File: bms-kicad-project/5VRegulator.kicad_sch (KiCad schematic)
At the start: 39 parts

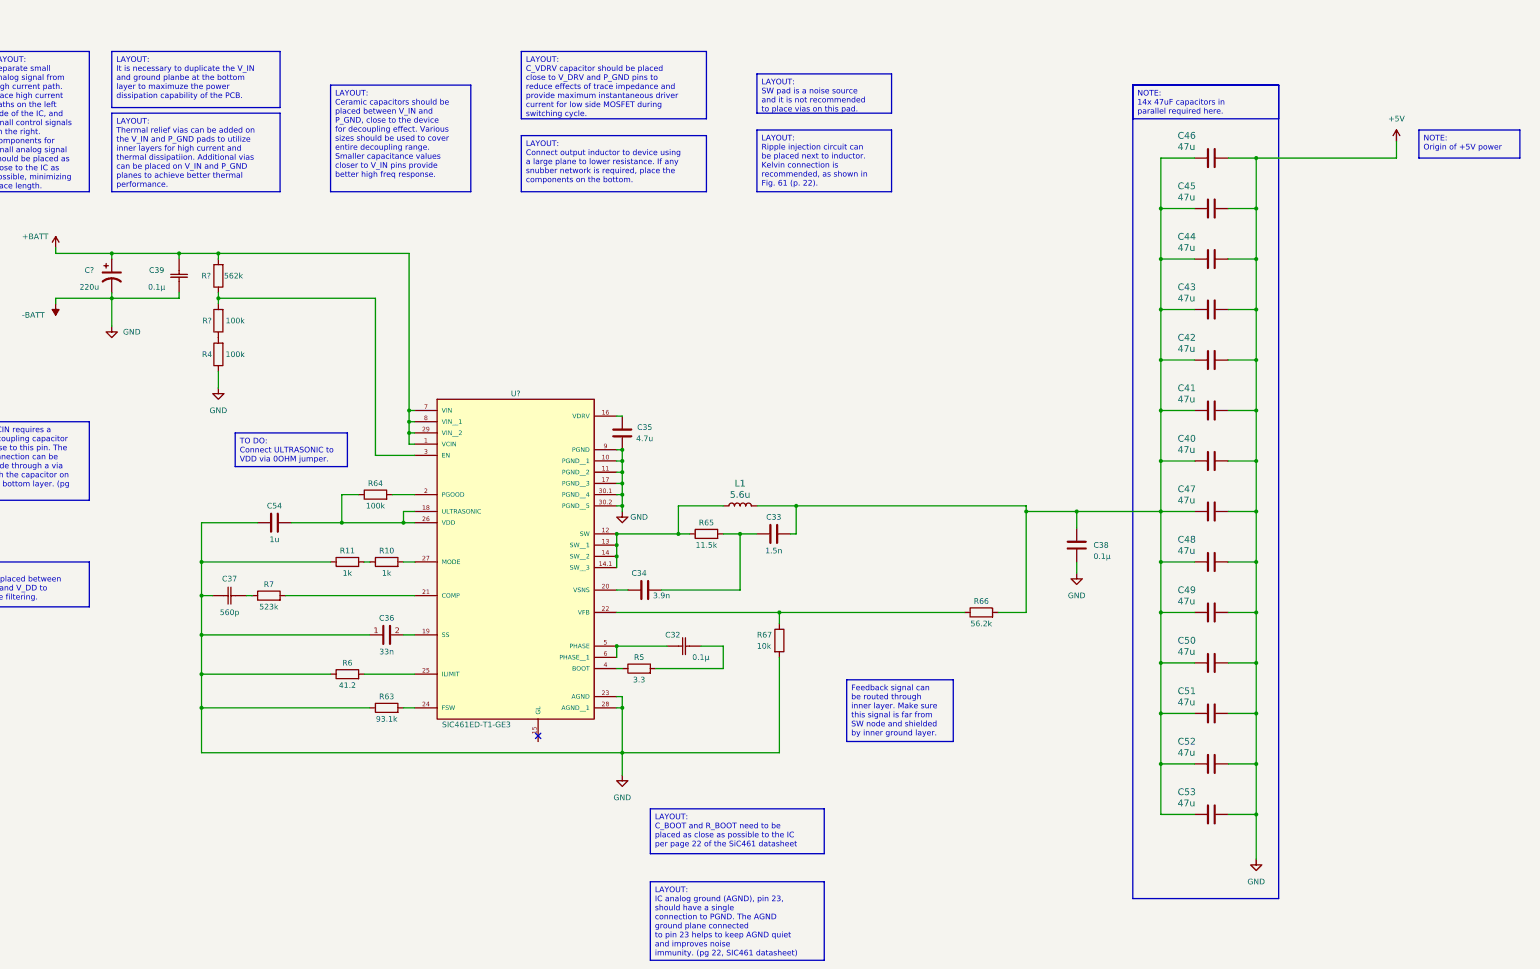
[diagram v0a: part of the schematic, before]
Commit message: feat: Added snubber circuit to 5V Regulator schematic
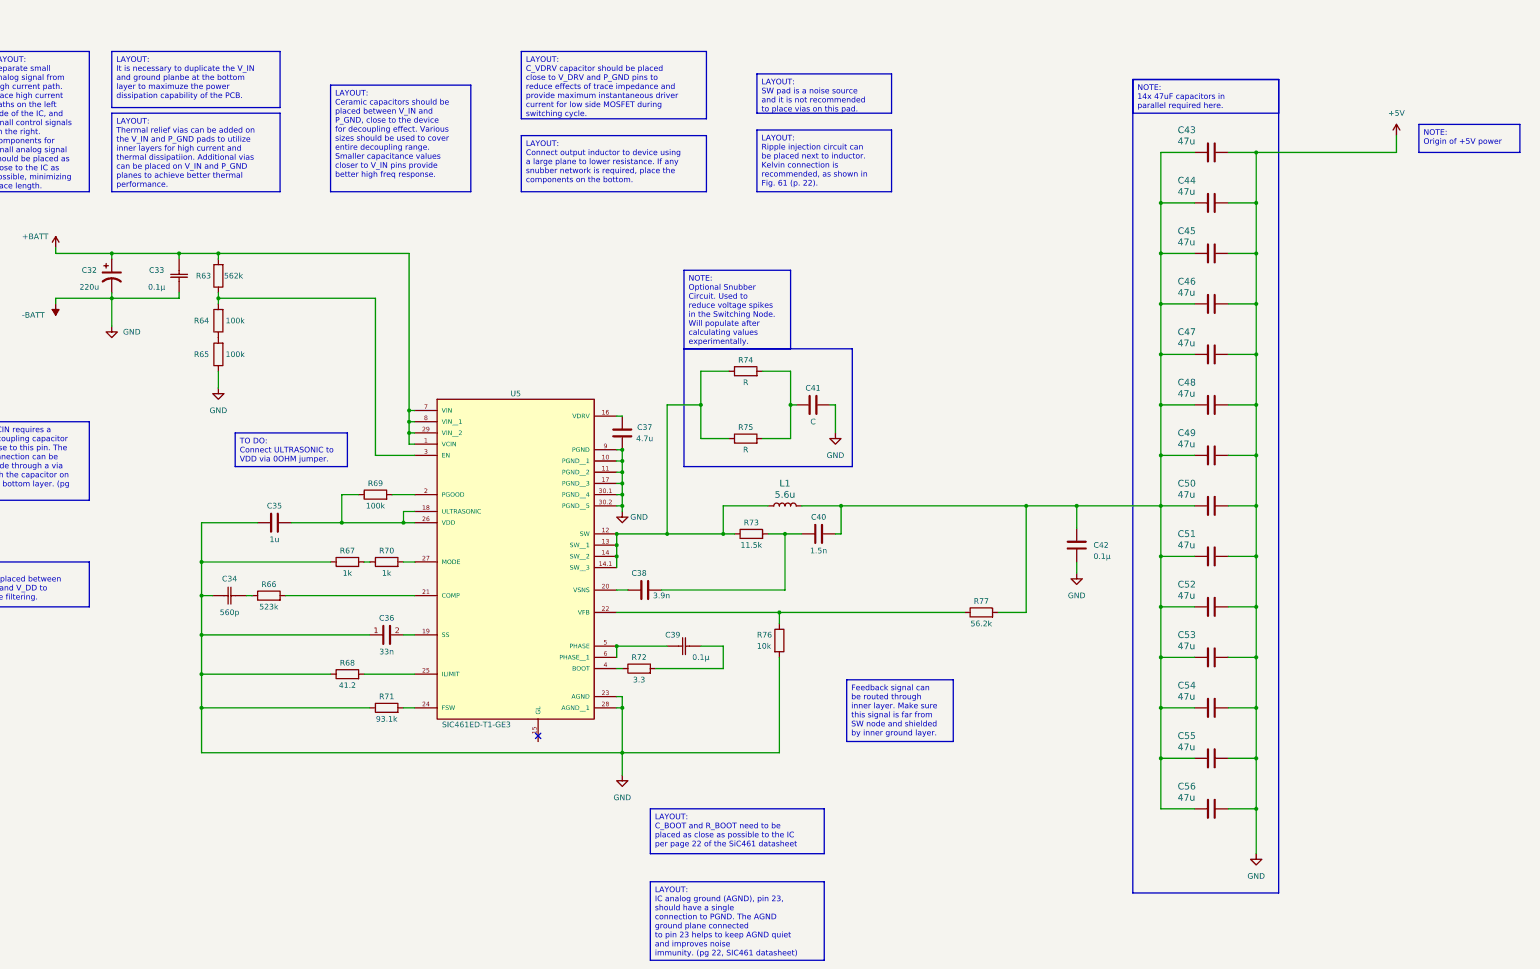
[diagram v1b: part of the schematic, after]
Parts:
- added C41: C, symbol Device:C
- added R74, R75: R, symbol Device:R
- gave numbers to parts that had none: 4
- renumbered C39 to C33, C37 to C34, C54 to C35, C35 to C37, C34 to C38, C32 to C39, C33 to C40, C38 to C42, C46 to C43, C45 to C44, C44 to C45, C43 to C46, C42 to C47, C41 to C48, C40 to C49, C47 to C50, C48 to C51, C49 to C52, C50 to C53, C51 to C54, C52 to C55, C53 to C56, R4 to R65, R7 to R66, R11 to R67, R6 to R68, R64 to R69, R10 to R70, R63 to R71, R5 to R72, R65 to R73, R67 to R76, R66 to R77
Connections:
- net +5V: now also C41.2
- net at L1.1, R73.1, U5.12 (SW)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: now also R74.1, R75.1
- new net: C41.1, R74.2, R75.2
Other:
- moved on the sheet: C40, C43, C44, C45, C46, C47, C48, C49, C50, C51, C52, C53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

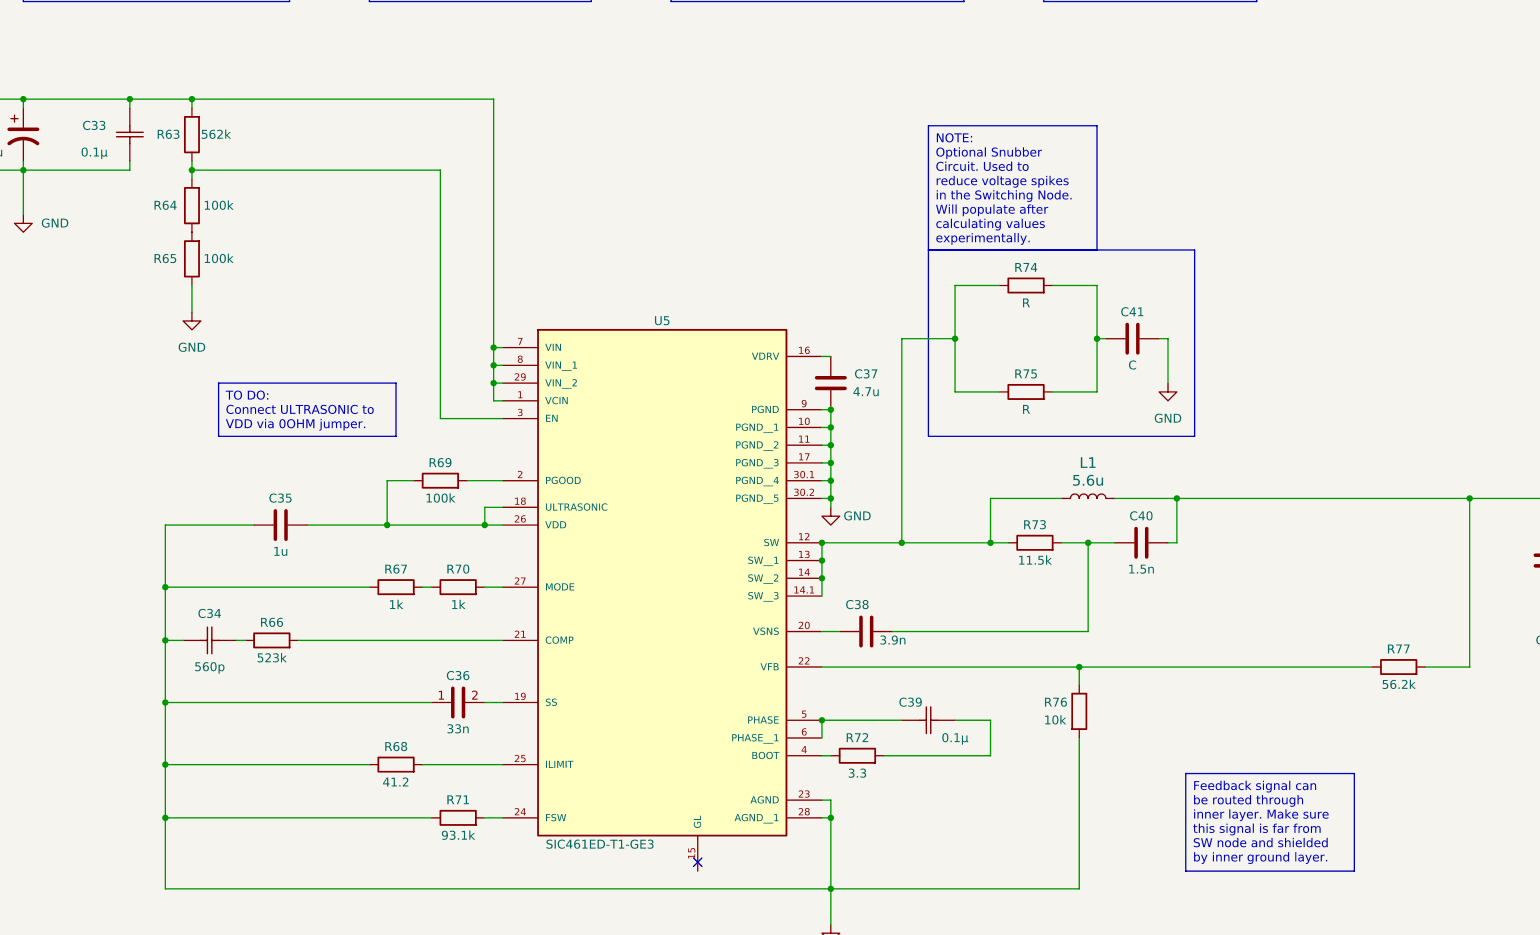
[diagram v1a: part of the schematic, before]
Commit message: feat: Added 0OHM jumper between ULTRASONIC and VDD, added LED indicator for PGOOD
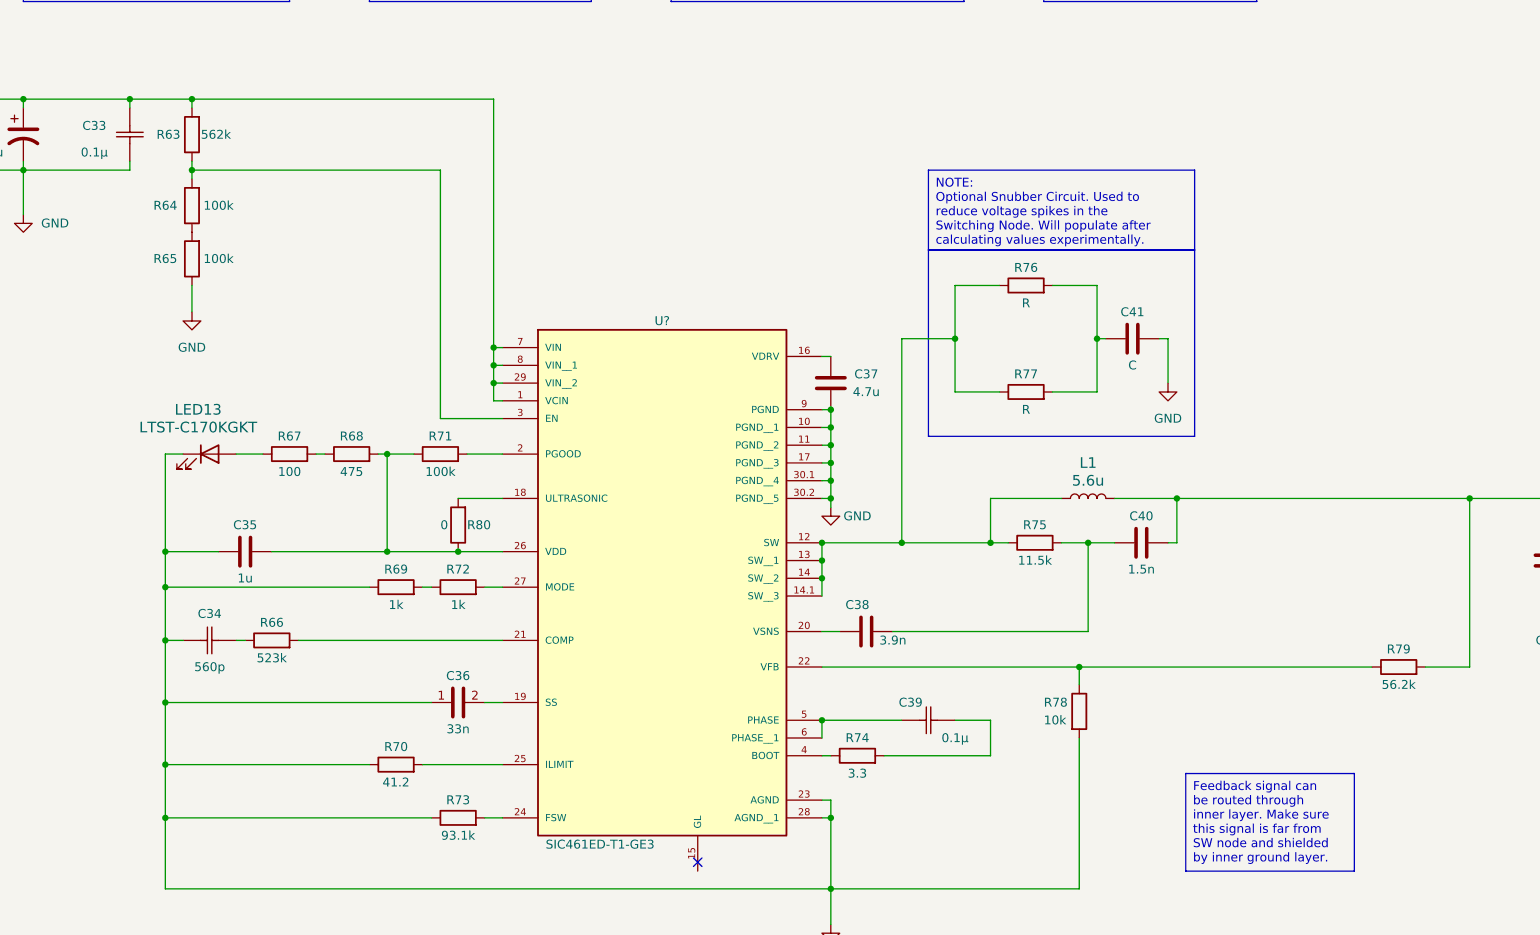
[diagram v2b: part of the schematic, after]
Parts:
- added LED13: LTST-C170KGKT, FixedWing:LED_LTST-C170KGKT_LTO, symbol FixedWing:LTST-C170KGKT
- added R67: 100, RESC2012X50N, symbol FixedWing:CRCW0805100RFKEA
- added R68: 475, RESC2012X50N, symbol FixedWing:CRCW0805475RFKEA
- added R80: 0, FixedWing:RC1206N_YAG, symbol FixedWing:RC1206JR-070RL
- C41: footprint (none) -> Capacitor_SMD:C_0805_2012Metric
- R63: footprint RC0805FR-07562KL:RESC2012X60N -> FixedWing:RESC2012X60N
- R73: renamed from R71; footprint FixedWing:RES_ERJ6ENF9312V -> FixedWing:RC0805N_PAN
- R76: renamed from R74; footprint (none) -> Resistor_SMD:R_0805_2012Metric
- R77: renamed from R75; footprint (none) -> Resistor_SMD:R_0805_2012Metric
- renumbered R67 to R69, R68 to R70, R69 to R71, R70 to R72, R72 to R74, R73 to R75, R76 to R78, R77 to R79, U5 to U?
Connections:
- net +5V: now also LED13.1 (K)
- net at C35.1, R71.1, U?.26 (VDD): now also R68.2, R80.1; no longer U?.18 (ULTRASONIC)
- new net: LED13.2 (A), R67.1
- new net: R67.2, R68.1
- new net: R80.2, U?.18 (ULTRASONIC)
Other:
- moved on the sheet: C35, R71

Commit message: feat: added buncha shit, refer to tasks 4 and 8
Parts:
- removed LED13: LTST-C170KGKT, FixedWing:LED_LTST-C170KGKT_LTO, symbol FixedWing:LTST-C170KGKT
- removed R67: 100, RESC2012X50N, symbol FixedWing:CRCW0805100RFKEA
- removed R68: 475, RESC2012X50N, symbol FixedWing:CRCW0805475RFKEA
- removed R71: 100k, FixedWing:RESC2012X60N, symbol FixedWing:RC0805FR-07100KL
- added LED13: LTST-C170KRKT, LEDC2012X120N, symbol FixedWing:LTST-C170KRKT
- added R88: 5.6k, FixedWing:RESC2012X60N, symbol FixedWing:RK73H2ATTD5601F
- gave numbers to parts that had none: 1
- renumbered C36 to C34, C34 to C36, L1 to L16, R63 to R84, R64 to R85, R65 to R86, R69 to R87, R72 to R89, R70 to R90, R73 to R91, R66 to R92, R80 to R93, R74 to R94, R78 to R95, R75 to R96, R76 to R97, R77 to R98, R79 to R99
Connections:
- net +5V: now also C40.2, C42.2, C43.2, C44.2, C45.2, C46.2, C47.2, C48.2, C49.2, C50.2, C51.2, C52.2, C53.2, C54.2, C55.2, C56.2, L16.2, R99.2; no longer C32.2, C33.2, C34.1, C35.2, C36.1, C37.1, C41.2, C42.1, C43.1, C44.1, C45.1, C46.1, C47.1, C48.1, C49.1, C50.1, C51.1, C52.1, C53.1, C54.1, C55.1, C56.1, R86.1, R87.1, R90.1, R91.1, R95.1, U5.10 (PGND__1), U5.11 (PGND__2), U5.17 (PGND__3), U5.23 (AGND), U5.28 (AGND__1), U5.30.1 (PGND__4), U5.30.2 (PGND__5), U5.9 (PGND)
- net at C35.1, R93.1, U5.26 (VDD): now also R88.1
- net at U5.2 (PGOOD): now also LED13.1 (K)
- new net GND: C32.2 (N), C33.2, C34.1, C35.2, C36.1, C37.1, C41.2, C42.1, C43.1, C44.1, C45.1, C46.1, C47.1, C48.1, C49.1, C50.1, C51.1, C52.1, C53.1, C54.1, C55.1, C56.1, LED13.2 (A), R86.1, R87.1, R88.2, R90.1, R91.1, R95.1, U5.10 (PGND__1), U5.11 (PGND__2), U5.17 (PGND__3), U5.23 (AGND), U5.28 (AGND__1), U5.30.1 (PGND__4), U5.30.2 (PGND__5), U5.9 (PGND)
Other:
- moved on the sheet: C33, C35, C36, C40, C41, L16, R84, R85, R86, R87, R89, R92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

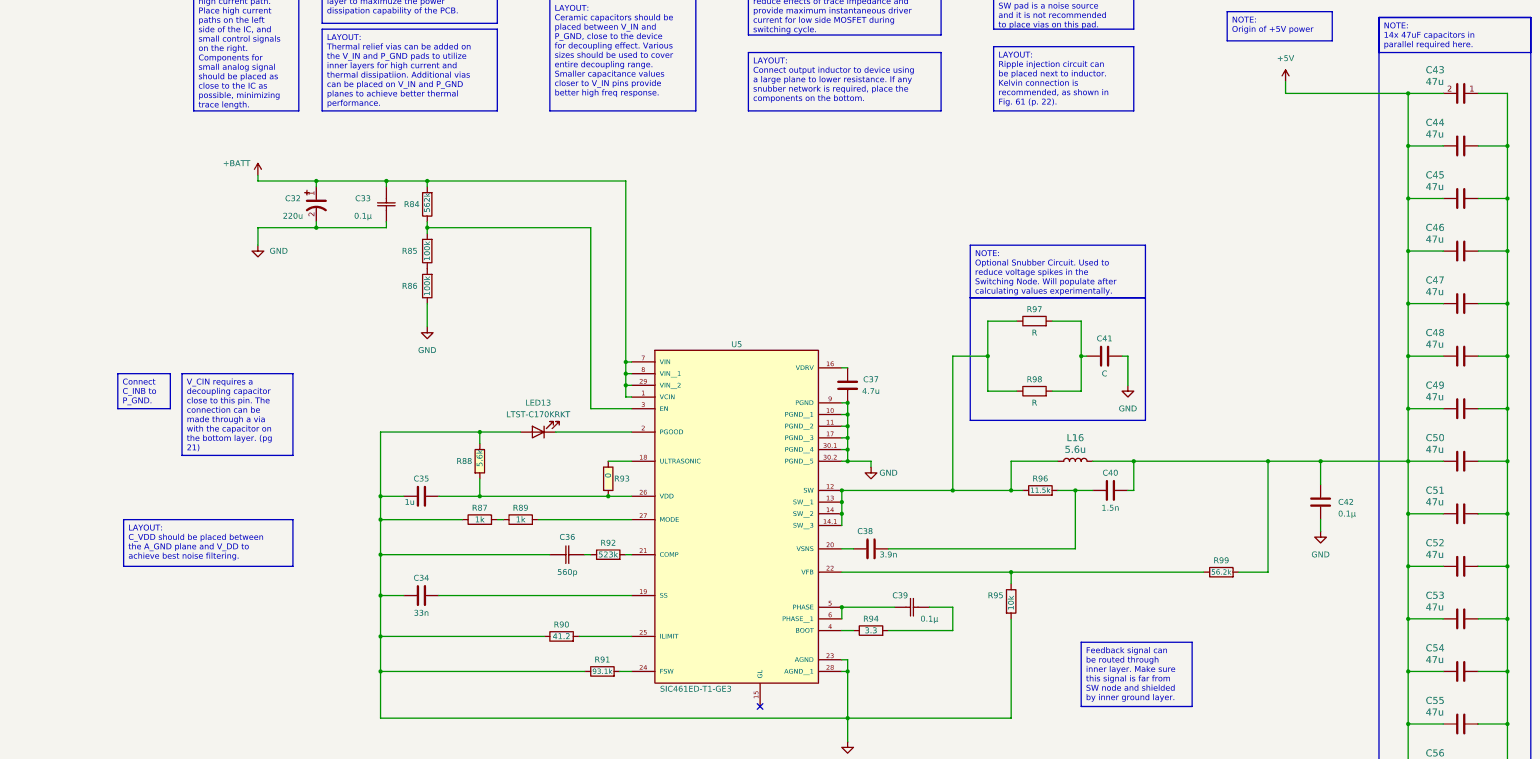
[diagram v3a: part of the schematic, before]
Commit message: feat: finished 5V reg circuit lgtm!
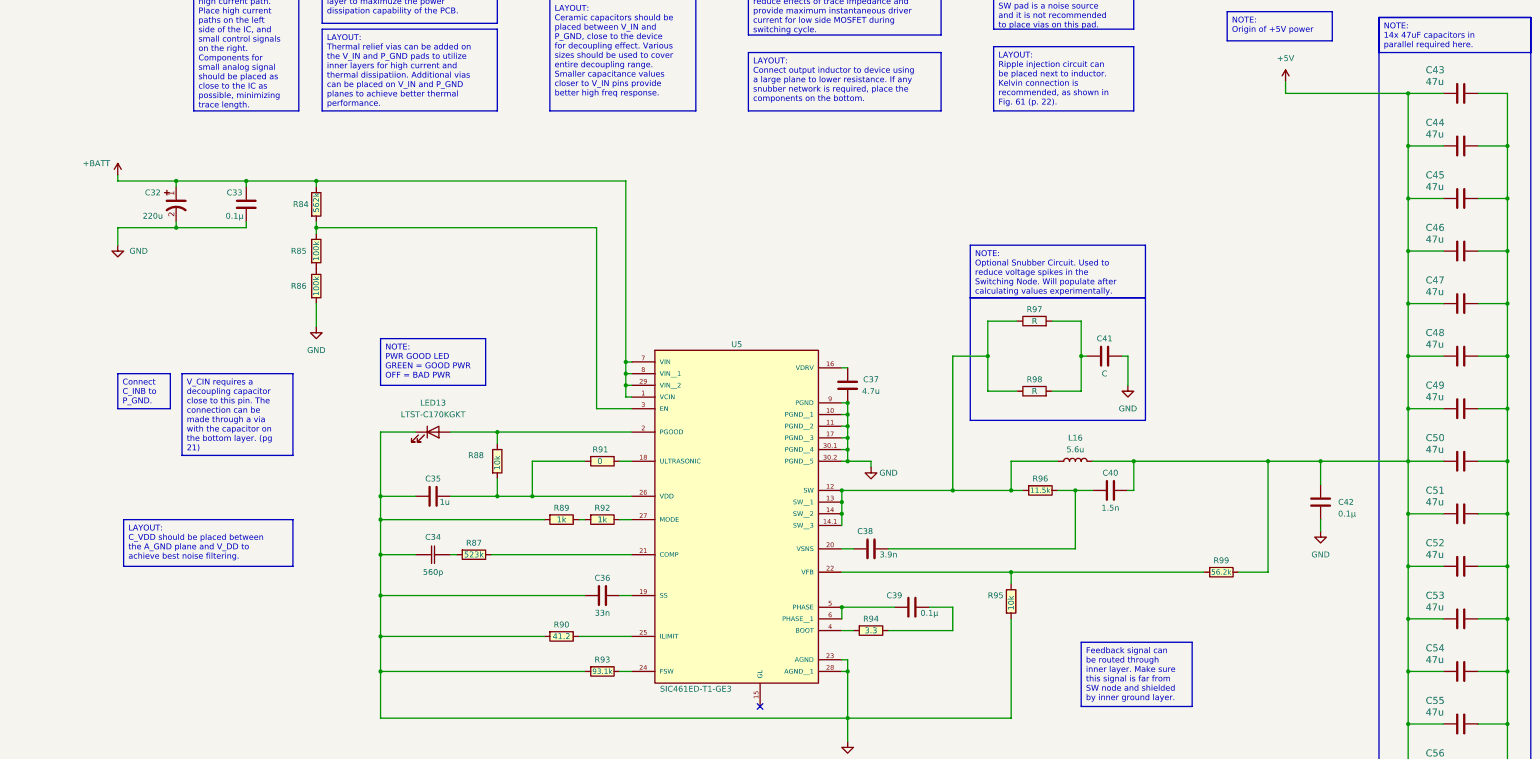
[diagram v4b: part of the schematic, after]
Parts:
- removed LED13: LTST-C170KRKT, LEDC2012X120N, symbol FixedWing:LTST-C170KRKT
- removed R88: 5.6k, FixedWing:RESC2012X60N, symbol FixedWing:RK73H2ATTD5601F
- removed R91: 93.1k, FixedWing:RC0805N_PAN, symbol FixedWing:ERJ6ENF9312V
- added LED13: LTST-C170KGKT, FixedWing:LED_LTST-C170KGKT_LTO, symbol FixedWing:LTST-C170KGKT
- added R88: 10k, FixedWing:KOA_Speer-RK73H2A-0-0-MFG, symbol FixedWing:RK73H2ATTD1002F
- added R93: 93.1k, FixedWing:RESC2012X60N, symbol FixedWing:RC0805FR-0793K1L
- renumbered C36 to C34, C34 to C36, R92 to R87, R87 to R89, R93 to R91, R89 to R92
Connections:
- net +BATT: now also C33.2; no longer C33.1
- net GND: now also C33.1, LED13.1 (K), R93.1; no longer C33.2
- net at U5.2 (PGOOD): now also LED13.2 (A), R88.2
- net at U5.24 (FSW): now also R93.2
- net at C35.1, R91.1, U5.26 (VDD): now also R88.1
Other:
- moved on the sheet: C32, C34, C35, C36, R91
